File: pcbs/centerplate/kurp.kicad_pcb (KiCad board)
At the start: 2 copper layers, 34 x 50 mm, 5 parts

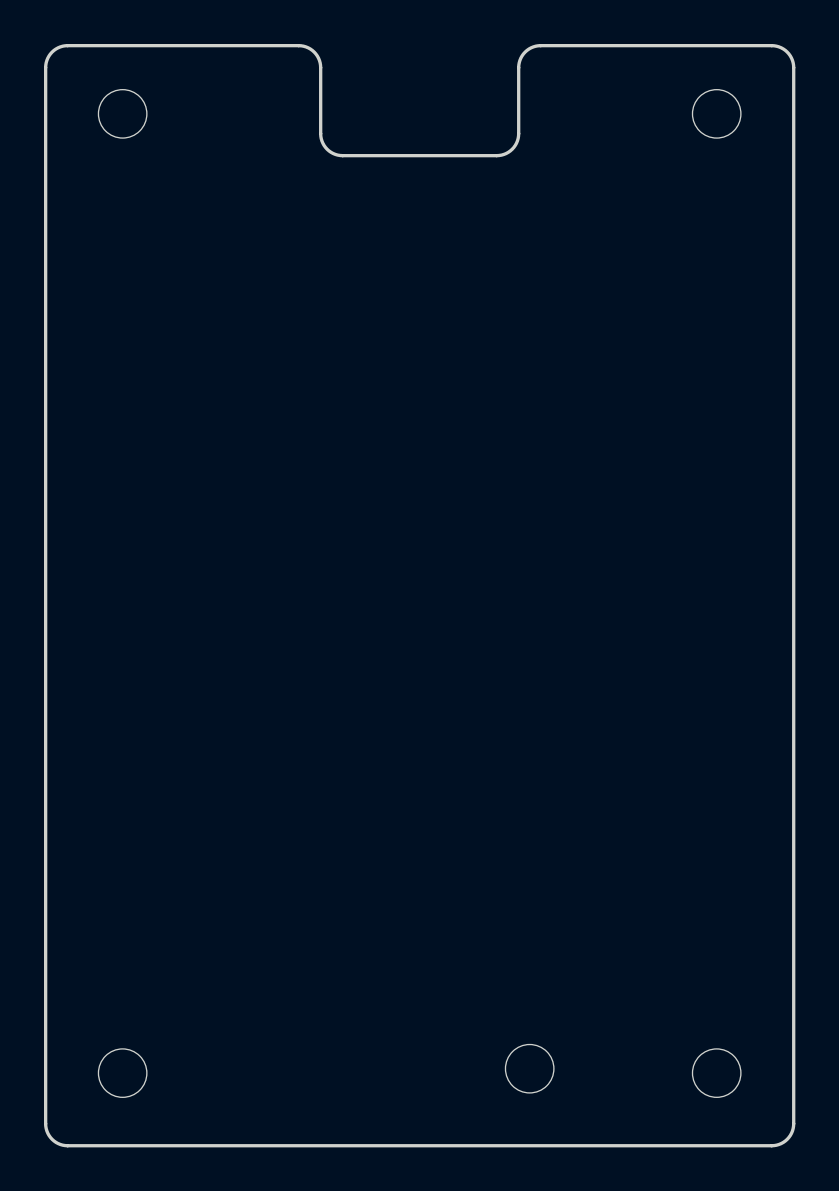
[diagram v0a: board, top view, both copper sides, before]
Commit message: widen cutout for oled/niceview
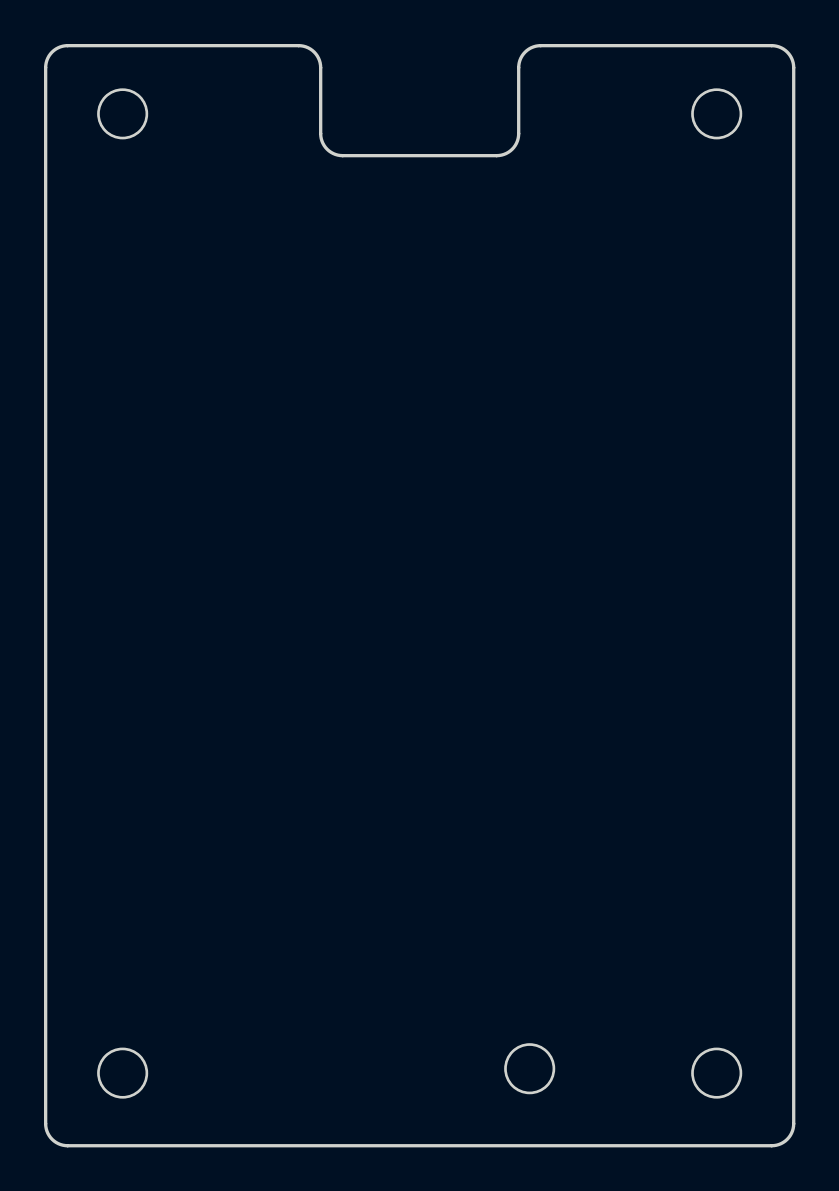
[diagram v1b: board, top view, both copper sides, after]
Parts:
- H1, H2, H3, H4, RESET1: footprint 0-jasonhazel-footprints:MountingHole_2.2mm_M2 -> 0-jasonhazel-footprints:MountingHole_2.2mm_M2_edgecut
